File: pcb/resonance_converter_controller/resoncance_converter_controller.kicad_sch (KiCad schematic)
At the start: 56 parts, among them J2 USB_C_Receptacle_USB2.0_14P, J4 Conn_02x19_Odd_Even, J5 Conn_01x02, J6 FX18-120S-0.8SH, J7 Conn_ARM_SWD_TagConnect_TC2030, U22 USBLC6-2P6

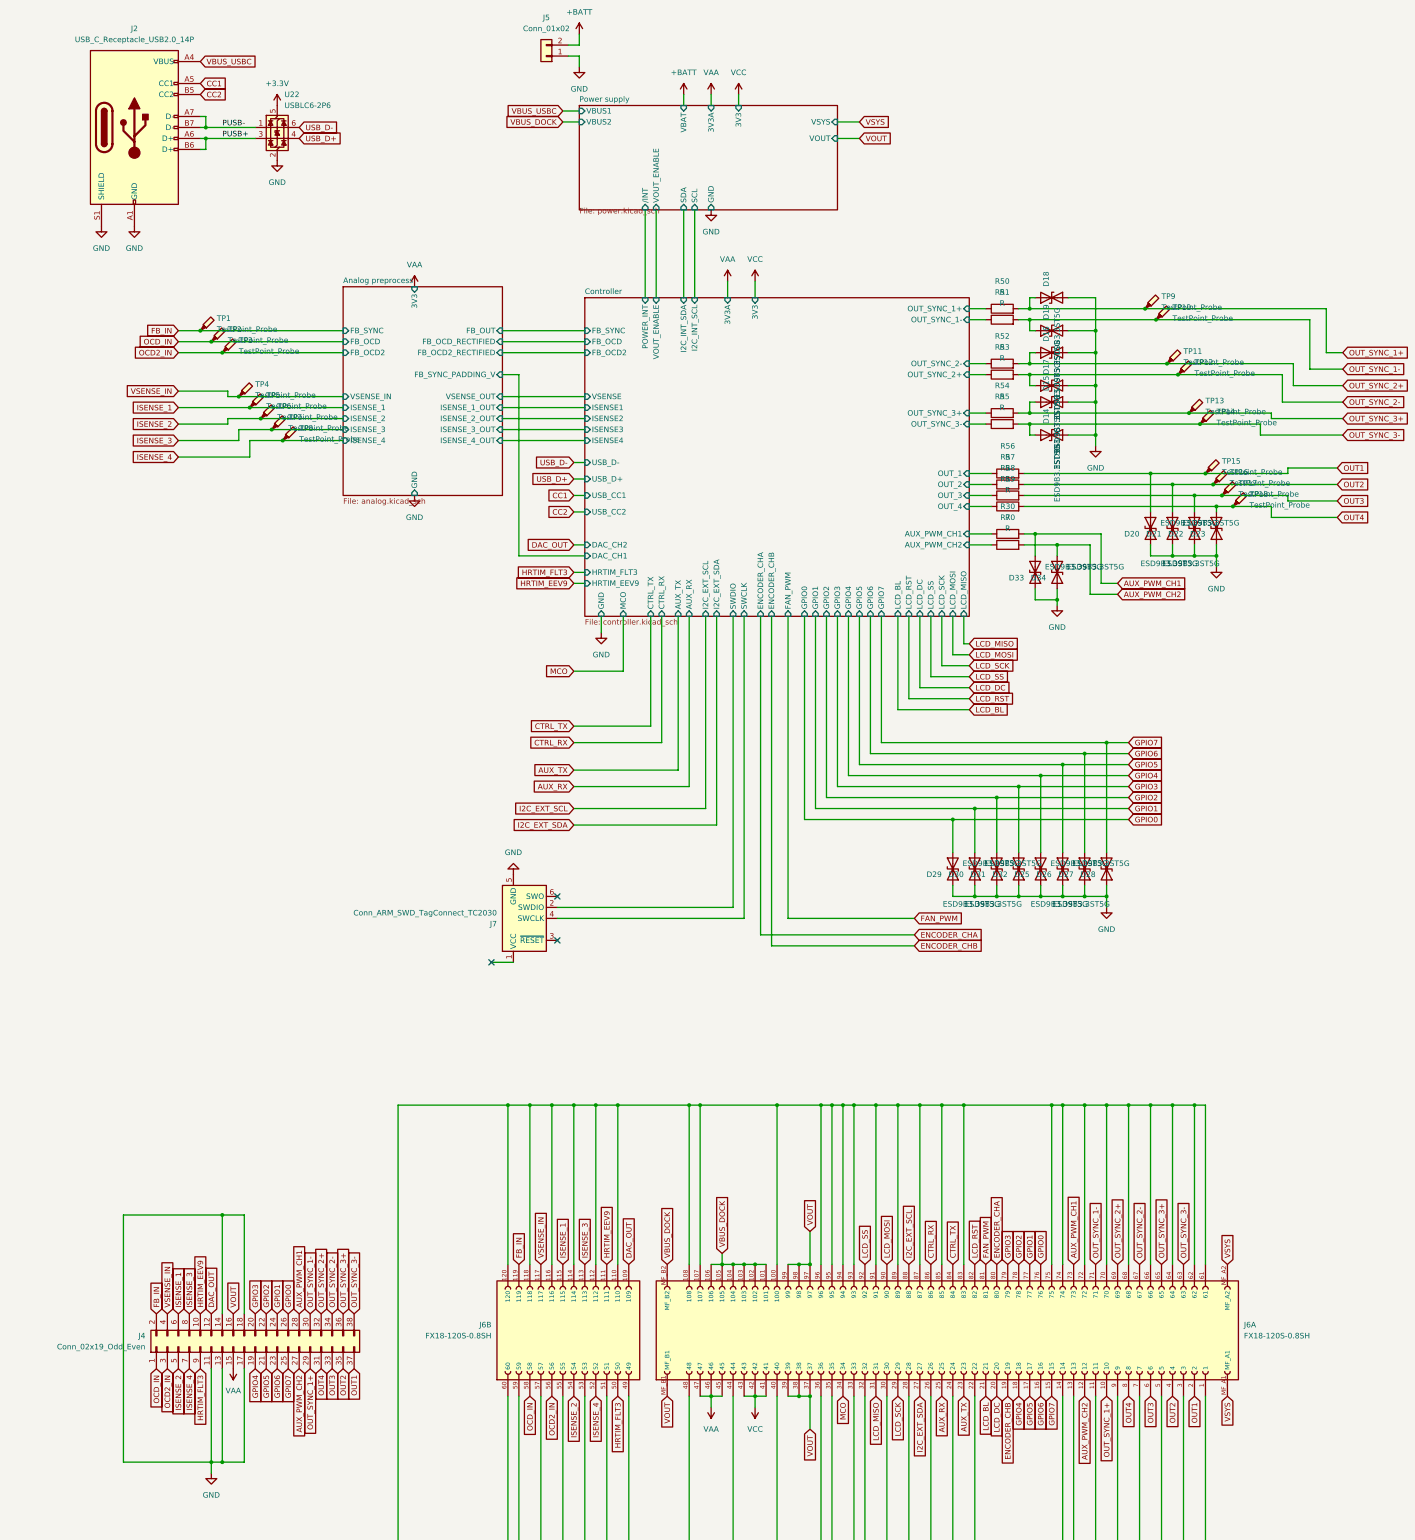
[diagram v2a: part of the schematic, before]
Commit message: Add mounting holes and some rework
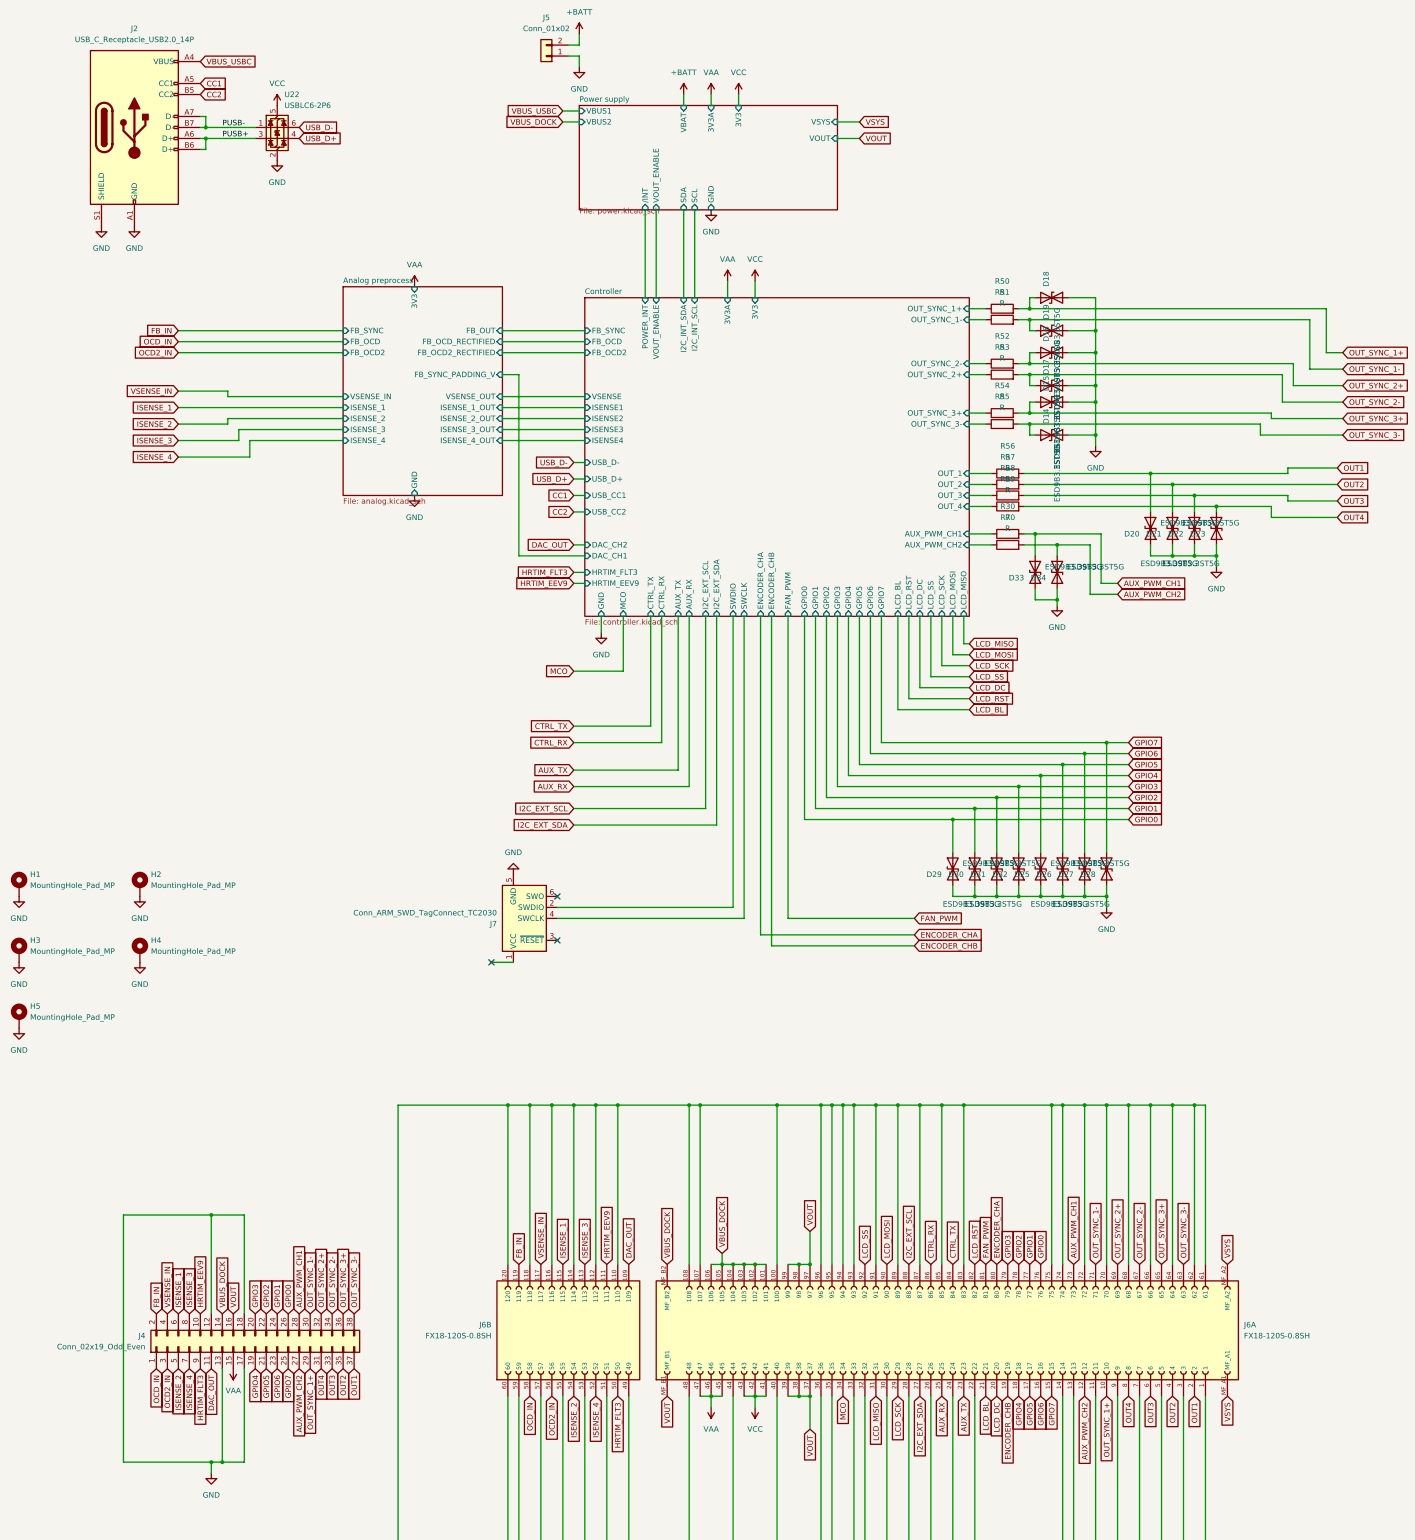
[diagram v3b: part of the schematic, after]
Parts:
- removed TP1, TP10, TP11, TP12, TP13, TP14, TP15, TP16, TP17, TP18, TP2, TP3, TP4, TP5, TP6, TP7, TP8, TP9: TestPoint_Probe, TestPoint:TestPoint_Pad_D2.0mm, symbol Connector:TestPoint_Probe
- added H1, H2, H3, H4, H5: MountingHole_Pad_MP, MountingHole:MountingHole_2.2mm_M2_Pad_Via, symbol Mechanical:MountingHole_Pad_MP
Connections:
- net +3.3V is gone; now on net VCC: U22.5 (VBUS)
- net DAC_OUT: now also J4.11 (Pin_11); no longer J4.12 (Pin_12)
- net GND: now also J4.12 (Pin_12), H1.MP, H2.MP, H3.MP, H4.MP, H5.MP; no longer J4.11 (Pin_11), J4.14 (Pin_14)
- net VBUS_DOCK: now also J4.14 (Pin_14)

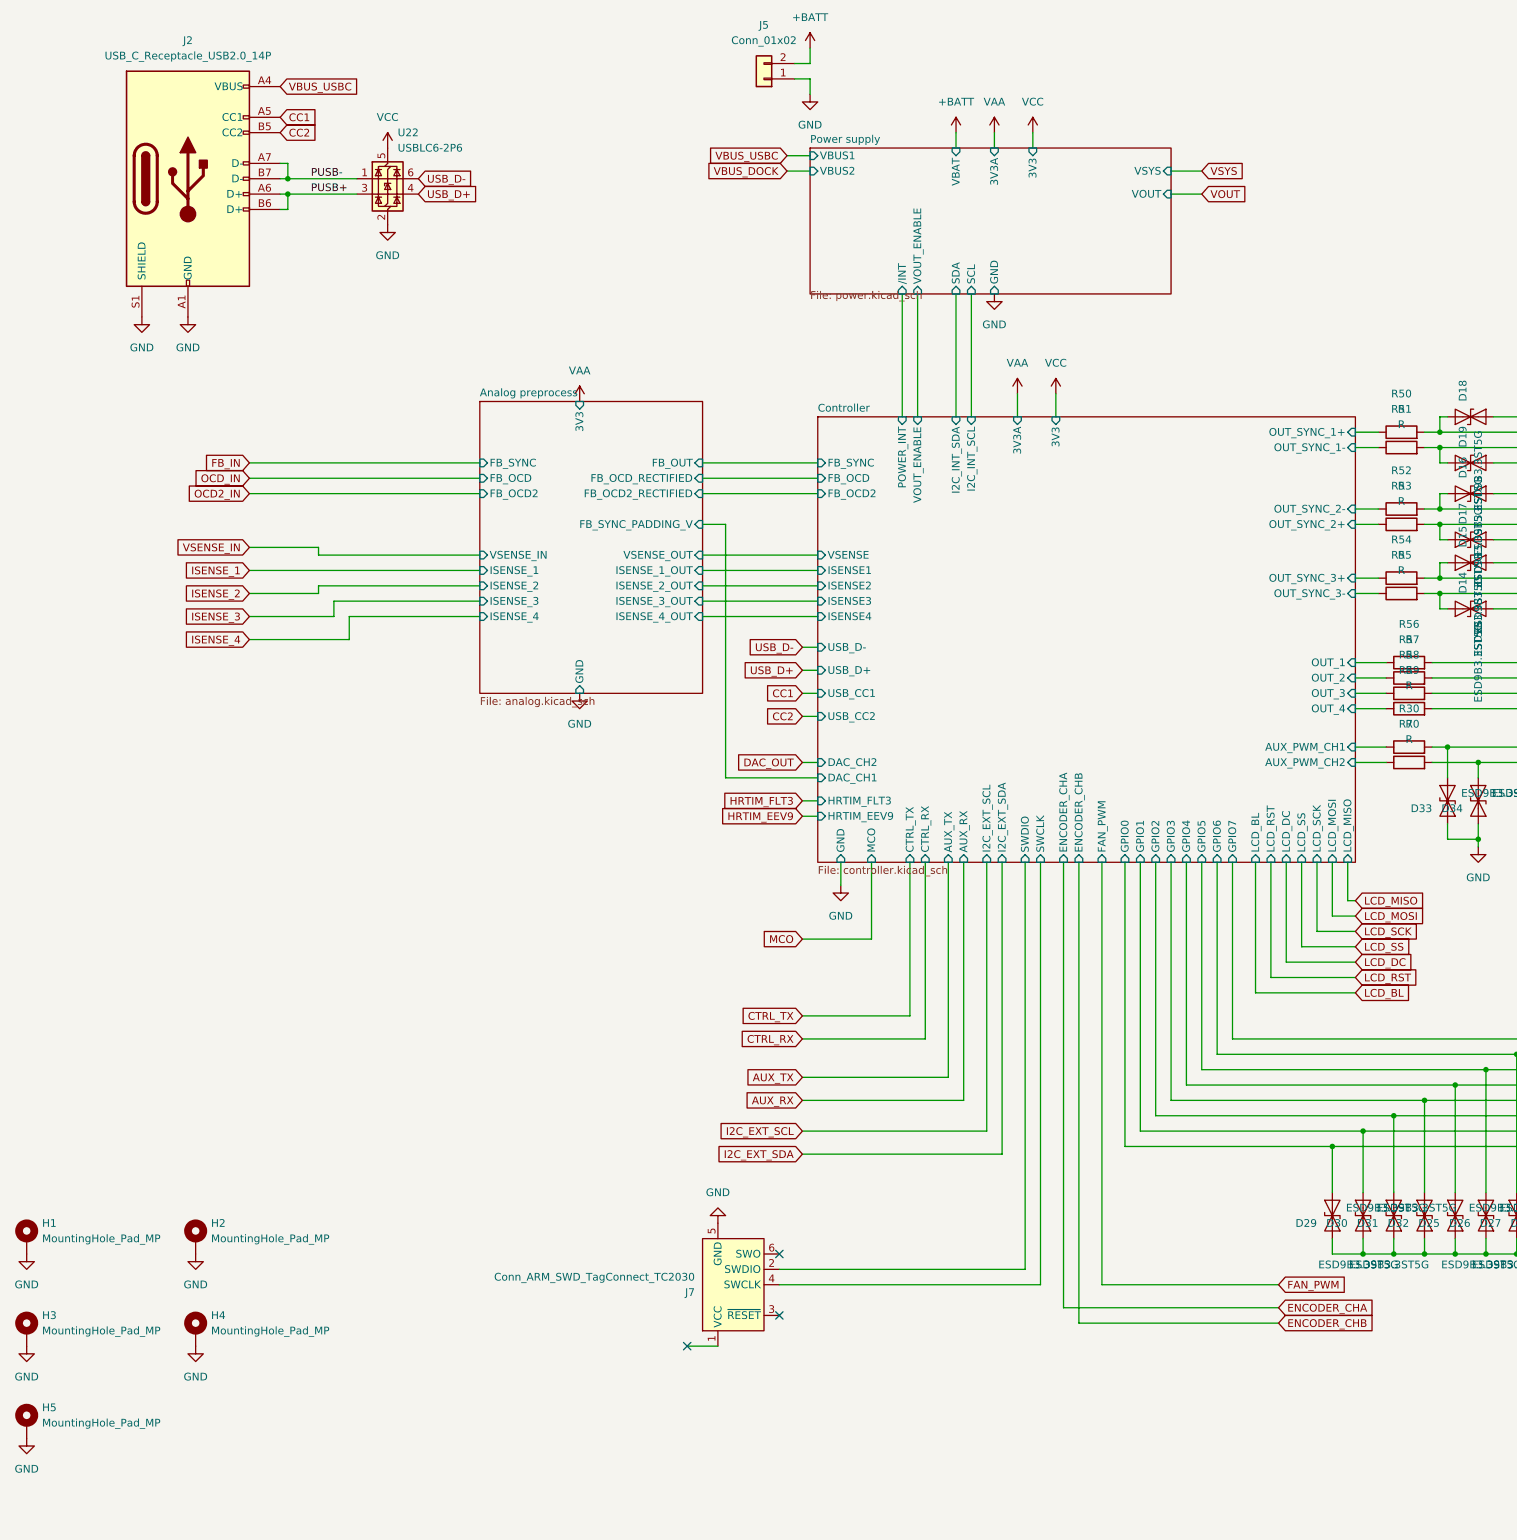
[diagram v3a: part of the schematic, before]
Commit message: Add reset handler buffer for dac and led
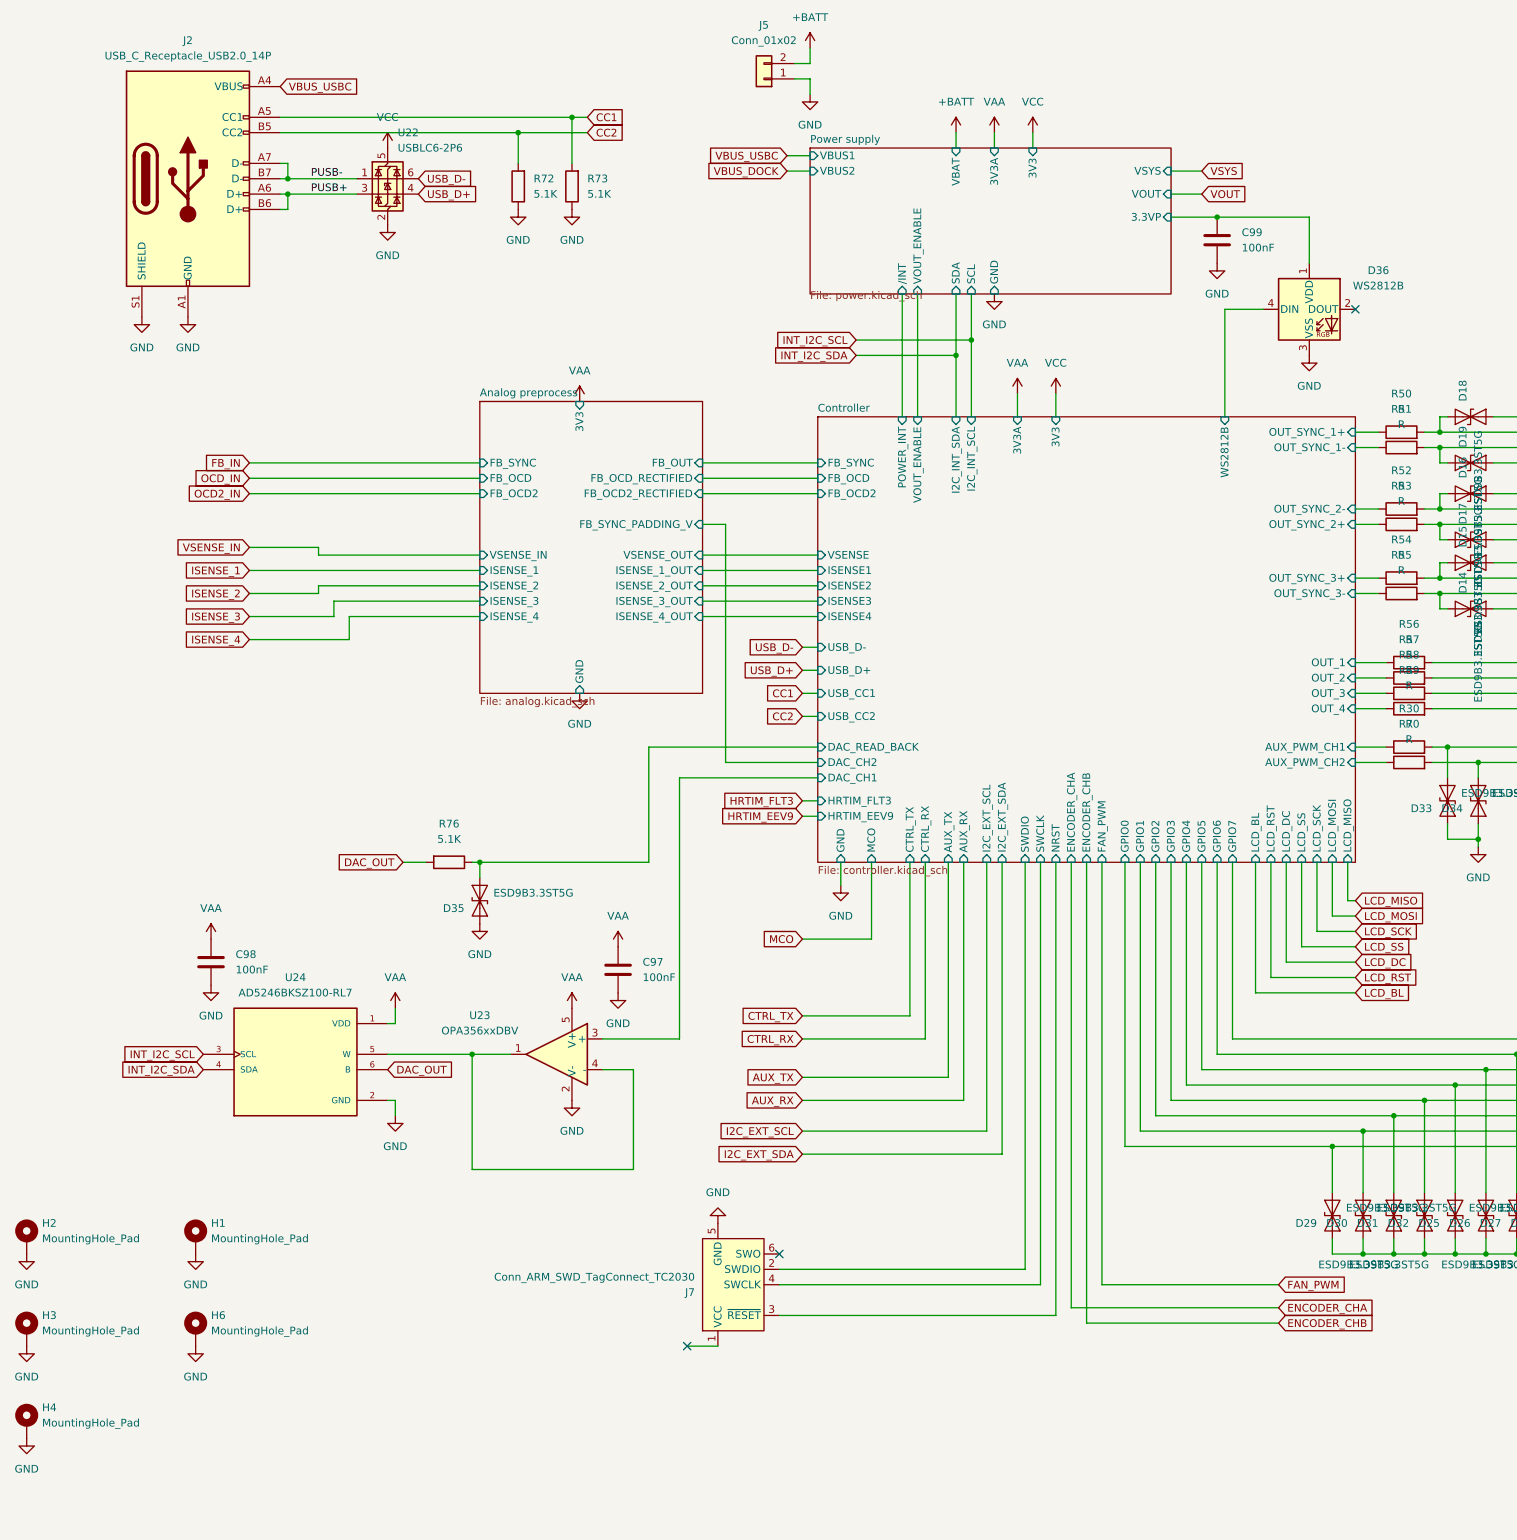
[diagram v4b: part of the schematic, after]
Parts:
- removed H1, H2, H3, H4, H5: MountingHole_Pad_MP, MountingHole:MountingHole_2.2mm_M2_Pad_Via, symbol Mechanical:MountingHole_Pad_MP
- added C97, C98, C99: 100nF, Capacitor_SMD:C_0402_1005Metric, symbol Device:C
- added D35: ESD9B3.3ST5G, Diode_SMD:D_SOD-923, symbol Diode:ESD9B3.3ST5G
- added D36: WS2812B, LED_SMD:LED_WS2812B-Mini_PLCC4_3.5x3.5mm, symbol LED:WS2812B
- added H1, H2, H3, H4, H6: MountingHole_Pad, MountingHole:MountingHole_2.2mm_M2_Pad_Via, symbol Mechanical:MountingHole_Pad
- added R72, R73, R76: 5.1K, Resistor_SMD:R_0402_1005Metric, symbol Device:R
- added U23: OPA356xxDBV, Package_TO_SOT_SMD:SOT-23-5, symbol Amplifier_Operational:OPA356xxDBV
- added U24: AD5246BKSZ100-RL7, AD5246BKSZ100-RL7:SOT65P210X110-6N, symbol AD5246BKSZ100-RL7:AD5246BKSZ100-RL7
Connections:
- net CC1: now also R73.2
- net CC2: now also R72.2
- net DAC_OUT: now also R76.2, U24.6 (B)
- net GND: now also C97.2, C98.2, C99.2, D35.2 (A2), D36.3 (VSS), H1.1, H2.1, H3.1, H4.1, H6.1, R72.1, R73.1, U23.2 (V-), U24.2 (GND)
- net VAA: now also C97.1, C98.1, U23.5 (V+), U24.1 (VDD)
- net Controller/NRST: now reaches J7.3 (~{RESET})
- new net: U23.1, U23.4 (-), U24.5 (W)
- new net Controller/DAC_CH1: U23.3 (+)
- new net Controller/DAC_READ_BACK: D35.1 (A1), R76.1
- new net Controller/WS2812B: D36.4 (DIN)
- new net INT_I2C_SCL: U24.3 (SCL)
- new net INT_I2C_SDA: U24.4 (SDA)
- new net Power supply/3.3VP: C99.1, D36.1 (VDD)
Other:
- sheet Controller ports: added DAC_READ_BACK, NRST, WS2812B; removed none
- sheet Power supply ports: added 3.3VP; removed none
